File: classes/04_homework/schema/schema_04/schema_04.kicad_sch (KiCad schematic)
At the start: 9 parts

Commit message: Export pdf diagram
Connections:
- net out | RESET is gone; now on net Vss: U=5V.9 (~{R}), U?.57 (PB5)
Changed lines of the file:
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@@
   (junction (at 179.07 58.42) (diameter 0) (color 0 0 0 0)
   )
+  (junction (at 101.6 26.67) (diameter 0) (color 0 0 0 0)
+  )
   (junction (at 252.73 90.17) (diameter 0) (color 0 0 0 0)
   )
@@
   (junction (at 179.07 26.67) (diameter 0) (color 0 0 0 0)
   )
+  (junction (at 101.6 99.06) (diameter 0) (color 0 0 0 0)
+  )
   (junction (at 179.07 43.18) (diameter 0) (color 0 0 0 0)
   )
@@
     (stroke (width 0) (type default) (color 0 0 0 0))
   )
-  (wire (pts (xy 71.12 99.06) (xy 146.05 99.06))
+  (wire (pts (xy 71.12 99.06) (xy 101.6 99.06))
     (stroke (width 0) (type default) (color 0 0 0 0))
   )
@@
     (stroke (width 0) (type default) (color 0 0 0 0))
   )
-  (wire (pts (xy 179.07 26.67) (xy 50.8 26.67))
+  (wire (pts (xy 179.07 26.67) (xy 101.6 26.67))
     (stroke (width 0) (type default) (color 0 0 0 0))
   )
@@
     (stroke (width 0) (type default) (color 0 0 0 0))
   )
+  (wire (pts (xy 101.6 99.06) (xy 146.05 99.06))
+    (stroke (width 0) (type default) (color 0 0 0 0))
+  )
   (wire (pts (xy 147.32 34.29) (xy 17.78 34.29))
     (stroke (width 0) (type default) (color 0 0 0 0))
   )
+  (wire (pts (xy 101.6 26.67) (xy 50.8 26.67))
+    (stroke (width 0) (type default) (color 0 0 0 0))
+  )
   (wire (pts (xy 173.99 106.68) (xy 182.88 106.68))
     (stroke (width 0) (type default) (color 0 0 0 0))
@@
   (polyline (pts (xy 189.23 30.48) (xy 152.4 30.48))
     (stroke (width 0) (type default) (color 0 0 0 0))
+  )
+  (wire (pts (xy 101.6 26.67) (xy 101.6 99.06))
+    (stroke (width 0) (type dot) (color 0 0 0 0))
   )
   (wire (pts (xy 173.99 115.57) (xy 215.9 115.57))
@@
     (effects (font (size 1.27 1.27)) (justify left bottom))
   )
+  (label "hard 1" (at 101.6 95.25 0)
+    (effects (font (size 1.27 1.27)) (justify left bottom))
+  )

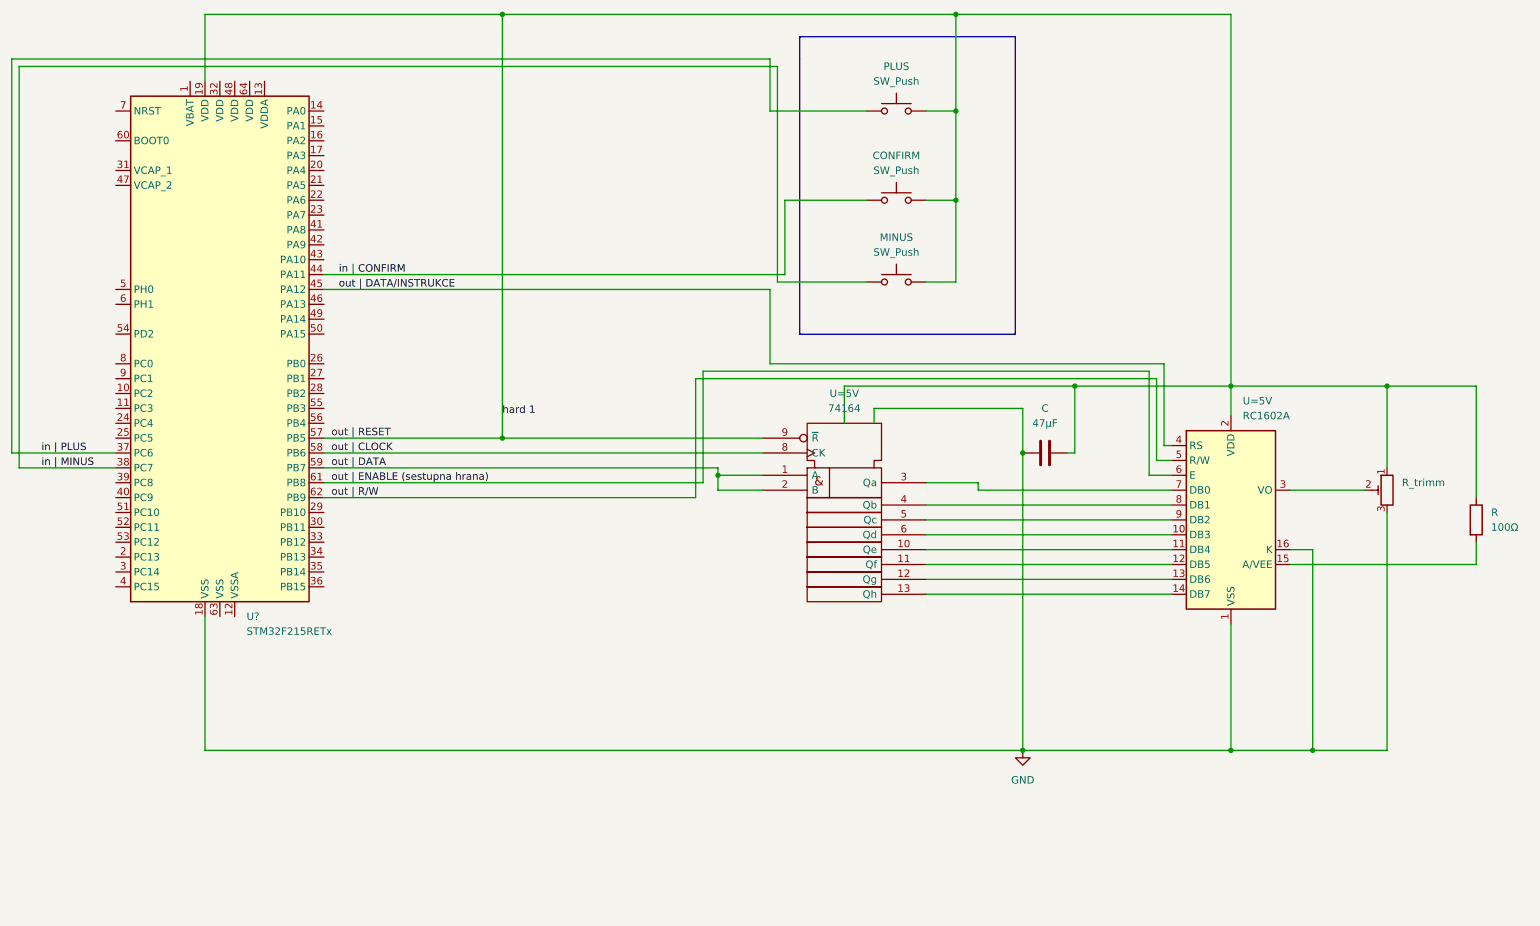
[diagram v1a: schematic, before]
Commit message: Config gates for UART
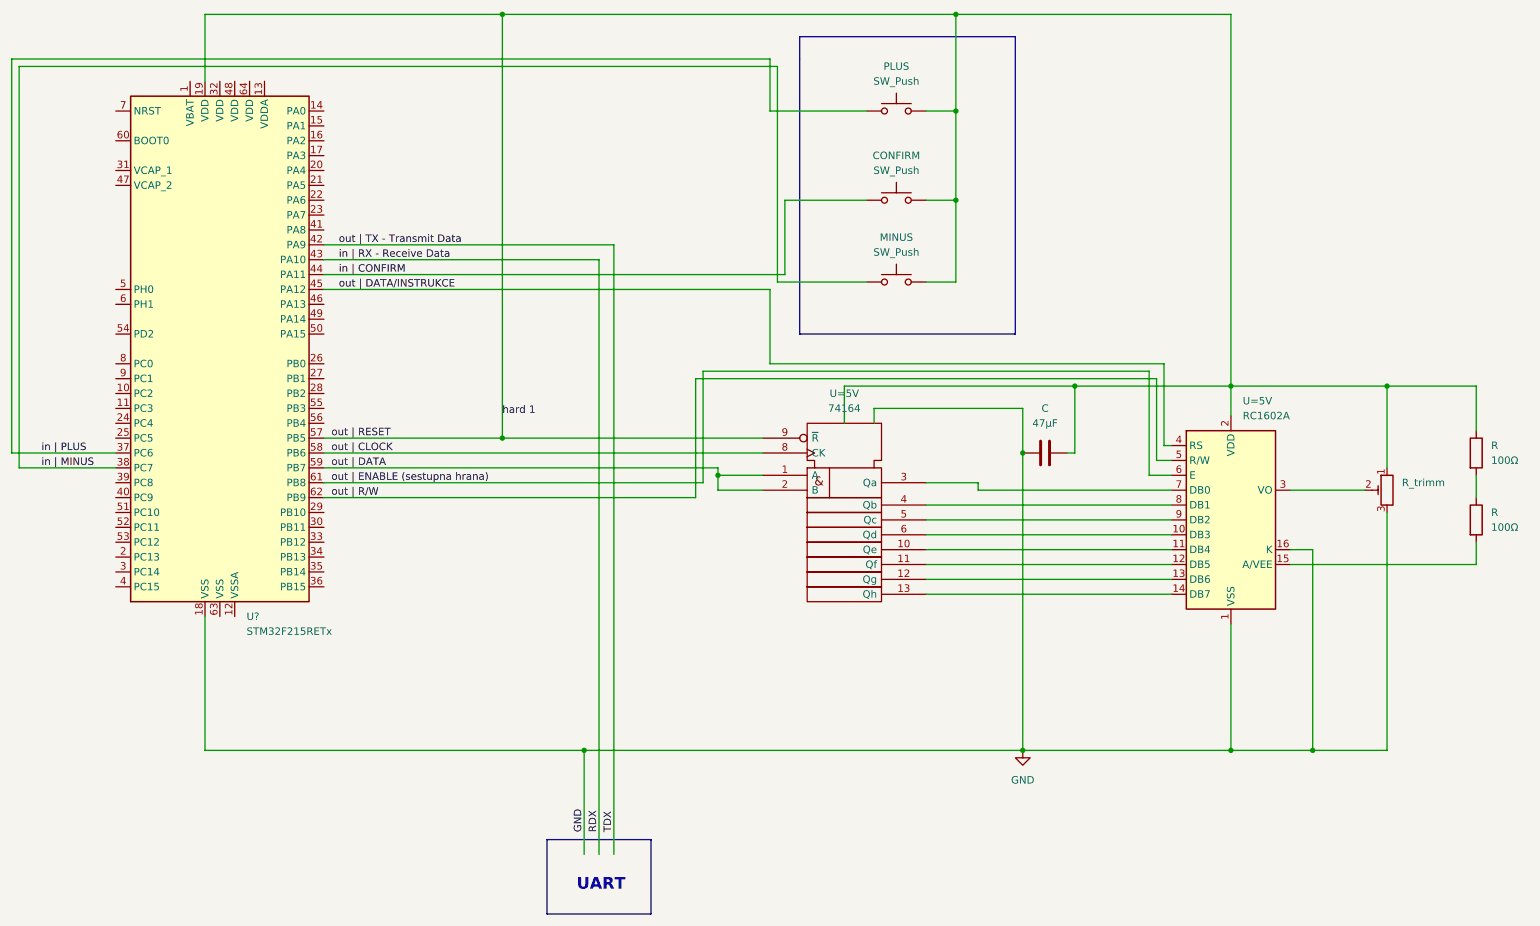
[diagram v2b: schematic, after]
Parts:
- added R: 100Ω, symbol Device:R
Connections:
- net Vss: now also R.1; no longer R.1
- net TDX: now reaches U?.42 (PA9)
- net RDX: now reaches U?.43 (PA10)
- new net: R.1, R.2
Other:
- note added: "UART"
- company: (none) -> kucerp28@fel.cvut.cz
- title: (none) -> Řídicí jednotka se zobrazovačem LCD a kanálem - UART
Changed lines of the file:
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@@
 (kicad_sch (version 20211123) (generator eeschema)
   (paper "A4")
+  (title_block
+    (title "Řídicí jednotka se zobrazovačem LCD a kanálem - UART")
+    (date "2022-11-21")
+    (company "kucerp28@fel.cvut.cz")
+  )
   (junction (at 179.07 58.42) (diameter 0) (color 0 0 0 0)
   )
   (junction (at 101.6 26.67) (diameter 0) (color 0 0 0 0)
   )
+  (junction (at 115.57 152.4) (diameter 0) (color 0 0 0 0)
+  )
   (junction (at 252.73 90.17) (diameter 0) (color 0 0 0 0)
   )
@@
     (stroke (width 0) (type default) (color 0 0 0 0))
   )
-  (wire (pts (xy 50.8 152.4) (xy 190.5 152.4))
+  (wire (pts (xy 50.8 152.4) (xy 115.57 152.4))
     (stroke (width 0) (type default) (color 0 0 0 0))
   )
@@
     (stroke (width 0) (type default) (color 0 0 0 0))
   )
-  (wire (pts (xy 267.97 109.22) (xy 267.97 90.17))
+  (wire (pts (xy 267.97 109.22) (xy 267.97 105.41))
     (stroke (width 0) (type default) (color 0 0 0 0))
   )
@@
     (stroke (width 0) (type default) (color 0 0 0 0))
   )
+  (wire (pts (xy 71.12 68.58) (xy 118.11 68.58))
+    (stroke (width 0) (type default) (color 0 0 0 0))
+  )
+  (polyline (pts (xy 127 180.34) (xy 109.22 180.34))
+    (stroke (width 0) (type default) (color 0 0 0 0))
+  )
   (wire (pts (xy 149.86 71.12) (xy 149.86 58.42))
     (stroke (width 0) (type default) (color 0 0 0 0))
@@
     (stroke (width 0) (type default) (color 0 0 0 0))
   )
+  (wire (pts (xy 71.12 66.04) (xy 120.65 66.04))
+    (stroke (width 0) (type default) (color 0 0 0 0))
+  )
   (wire (pts (xy 190.5 101.6) (xy 190.5 152.4))
     (stroke (width 0) (type default) (color 0 0 0 0))
@@
     (stroke (width 0) (type default) (color 0 0 0 0))
   )
+  (wire (pts (xy 120.65 66.04) (xy 120.65 170.18))
+    (stroke (width 0) (type default) (color 0 0 0 0))
+  )
   (wire (pts (xy 138.43 104.14) (xy 138.43 105.41))
     (stroke (width 0) (type default) (color 0 0 0 0))
@@
     (stroke (width 0) (type default) (color 0 0 0 0))
   )
+  (polyline (pts (xy 109.22 167.64) (xy 109.22 180.34))
+    (stroke (width 0) (type default) (color 0 0 0 0))
+  )
   (wire (pts (xy 146.05 107.95) (xy 138.43 107.95))
     (stroke (width 0) (type default) (color 0 0 0 0))
@@
     (stroke (width 0) (type default) (color 0 0 0 0))
   )
+  (wire (pts (xy 118.11 68.58) (xy 118.11 170.18))
+    (stroke (width 0) (type default) (color 0 0 0 0))
+  )
   (wire (pts (xy 173.99 43.18) (xy 179.07 43.18))
     (stroke (width 0) (type default) (color 0 0 0 0))
@@
     (stroke (width 0) (type default) (color 0 0 0 0))
   )
+  (polyline (pts (xy 127 167.64) (xy 127 180.34))
+    (stroke (width 0) (type default) (color 0 0 0 0))
+  )
+  (wire (pts (xy 267.97 97.79) (xy 267.97 90.17))
+    (stroke (width 0) (type default) (color 0 0 0 0))
+  )
+  (wire (pts (xy 115.57 152.4) (xy 190.5 152.4))
+    (stroke (width 0) (type default) (color 0 0 0 0))
+  )
   (wire (pts (xy 226.06 26.67) (xy 226.06 90.17))
     (stroke (width 0) (type default) (color 0 0 0 0))
@@
     (stroke (width 0) (type default) (color 0 0 0 0))
   )
+  (polyline (pts (xy 109.22 167.64) (xy 127 167.64))
+    (stroke (width 0) (type default) (color 0 0 0 0))
+  )
   (wire (pts (xy 179.07 58.42) (xy 179.07 72.39))
+    (stroke (width 0) (type default) (color 0 0 0 0))
+  )
+  (wire (pts (xy 115.57 152.4) (xy 115.57 170.18))
     (stroke (width 0) (type default) (color 0 0 0 0))
   )
@@
     )
   )
+  (text "UART" (at 114.3 176.53 0)
+    (effects (font (size 2 2) (thickness 0.4) bold) (justify left bottom))
+  )
   (label "in | PLUS" (at 22.86 101.6 0)
     (effects (font (size 1.27 1.27)) (justify left bottom))
   )
+  (label "RDX" (at 118.11 166.37 90)
+    (effects (font (size 1.27 1.27)) (justify left bottom))
+  )
+  (label "out | TX - Transmit Data" (at 73.66 66.04 0)
+    (effects (font (size 1.27 1.27)) (justify left bottom))
+  )
   (label "out | CLOCK" (at 72.39 101.6 0)
     (effects (font (size 1.27 1.27)) (justify left bottom))
@@
     (effects (font (size 1.27 1.27)) (justify left bottom))
   )
+  (label "in | RX - Receive Data" (at 73.66 68.58 0)
+    (effects (font (size 1.27 1.27)) (justify left bottom))
+  )
+  (label "GND" (at 115.57 166.37 90)
+    (effects (font (size 1.27 1.27)) (justify left bottom))
+  )
   (label "out | RESET" (at 72.39 99.06 0)
     (effects (font (size 1.27 1.27)) (justify left bottom))
@@
   )
   (label "out | DATA" (at 72.39 104.14 0)
+    (effects (font (size 1.27 1.27)) (justify left bottom))
+  )
+  (label "TDX" (at 120.65 166.37 90)
     (effects (font (size 1.27 1.27)) (justify left bottom))
   )
@@
     )
     (property "Datasheet" "~" (id 3) (at 168.91 38.1 0)
+      (effects (font (size 1.27 1.27)) hide)
+    )
+    (pin "1")
+    (pin "2")
+  )
+  (symbol (lib_id "Device:R") (at 267.97 101.6 0) (unit 1)
+    (in_bom yes) (on_board yes) (fields_autoplaced)
+    (property "Reference" "R" (id 0) (at 270.51 100.3299 0)
+      (effects (font (size 1.27 1.27)) (justify left))
+    )
+    (property "Value" "100Ω" (id 1) (at 270.51 102.8699 0)
+      (effects (font (size 1.27 1.27)) (justify left))
+    )
+    (property "Footprint" "" (id 2) (at 266.192 101.6 90)
+      (effects (font (size 1.27 1.27)) hide)
+    )
+    (property "Datasheet" "~" (id 3) (at 267.97 101.6 0)
       (effects (font (size 1.27 1.27)) hide)
     )
@@
       (reference "R") (unit 1) (value "100Ω") (footprint "")
     )
+    (path "/674a4e8d-7816-4cf1-817e-074c81609878"
+      (reference "R") (unit 1) (value "100Ω") (footprint "")
+    )
